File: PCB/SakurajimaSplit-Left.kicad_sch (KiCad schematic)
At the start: 14 parts, among them J1 SWD, J2 USB_C_Receptacle_USB2.0_16P, J3 USB_C_Receptacle_USB2.0_16P, SW22 SW_Push, U1 USBLC6-2SC6, U2 STM32G0B1CBT6, Y1 8MHz

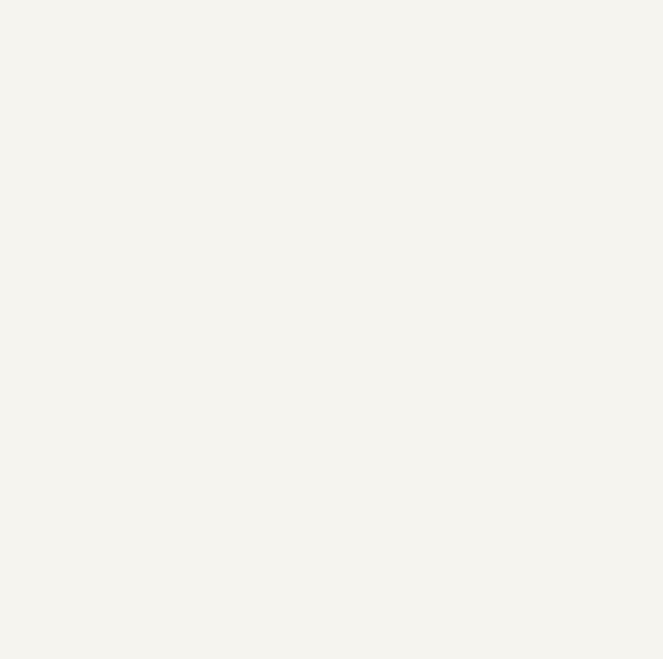
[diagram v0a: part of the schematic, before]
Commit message: feat(schematic): add key matrix
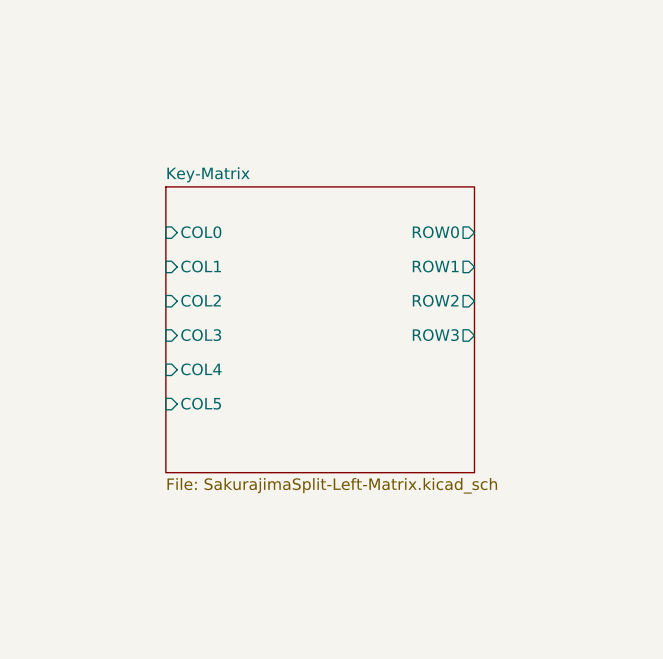
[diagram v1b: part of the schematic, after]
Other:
- added sheet Key-Matrix (SakurajimaSplit-Left-Matrix.kicad_sch)
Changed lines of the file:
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@@
+		)
+	)
+	(sheet
+		(at 227.33 109.22)
+		(size 34.29 31.75)
+		(exclude_from_sim no)
+		(in_bom yes)
+		(on_board yes)
+		(dnp no)
+		(fields_autoplaced yes)
+		(stroke
+			(width 0.1524)
+			(type solid)
+		)
+		(fill
+			(color 0 0 0 0.0000)
+		)
+		(property "Sheetname" "Key-Matrix"
+			(at 227.33 108.5084 0)
+			(effects
+				(font
+					(size 1.27 1.27)
+				)
+				(justify left bottom)
+			)
+		)
+		(property "Sheetfile" "SakurajimaSplit-Left-Matrix.kicad_sch"
+			(at 227.33 141.5546 0)
+			(effects
+				(font
+					(size 1.27 1.27)
+				)
+				(justify left top)
+			)
+		)
+		(pin "ROW0" output
+			(at 261.62 114.3 0)
+			(effects
+				(font
+					(size 1.27 1.27)
+				)
+				(justify right)
+			)
+		)
+		(pin "ROW1" output
+			(at 261.62 118.11 0)
+			(effects
+				(font
+					(size 1.27 1.27)
+				)
+				(justify right)
+			)
+		)
+		(pin "ROW2" output
+			(at 261.62 121.92 0)
+			(effects
+				(font
+					(size 1.27 1.27)
+				)
+				(justify right)
+			)
+		)
+		(pin "ROW3" output
+			(at 261.62 125.73 0)
+			(effects
+				(font
+					(size 1.27 1.27)
+				)
+				(justify right)
+			)
+		)
+		(pin "COL0" input
+			(at 227.33 114.3 180)
+			(effects
+				(font
+					(size 1.27 1.27)
+				)
+				(justify left)
+			)
+		)
+		(pin "COL1" input
+			(at 227.33 118.11 180)
+			(effects
+				(font
+					(size 1.27 1.27)
+				)
+				(justify left)
+			)
+		)
+		(pin "COL2" input
+			(at 227.33 121.92 180)
+			(effects
+				(font
+					(size 1.27 1.27)
+				)
+				(justify left)
+			)
+		)
+		(pin "COL3" input
+			(at 227.33 125.73 180)
+			(effects
+				(font
+					(size 1.27 1.27)
+				)
+				(justify left)
+			)
+		)
+		(pin "COL4" input
+			(at 227.33 129.54 180)
+			(effects
+				(font
+					(size 1.27 1.27)
+				)
+				(justify left)
+			)
+		)
+		(pin "COL5" input
+			(at 227.33 133.35 180)
+			(effects
+				(font
+					(size 1.27 1.27)
+				)
+				(justify left)
+			)
+		)
+		(instances
+			(project "SakurajimaSplit"
+				(path "/2049b6de-7453-46e1-ab60-70116abff9d6/d08add9a-e5d5-49be-809e-a90adb11436d"
+					(page "4")
+				)
+			)
 		)
 	)

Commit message: feat(sch): add host USB connection and power circuit
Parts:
- removed J2: USB_C_Receptacle_USB2.0_16P, symbol Connector:USB_C_Receptacle_USB2.0_16P
- removed R2, R3: 5.1k, symbol Device:R
- removed U1: USBLC6-2SC6, Package_TO_SOT_SMD:SOT-23-6, symbol Power_Protection:USBLC6-2SC6
- C1: renamed from C4; value C -> 20pF
- C2: renamed from C5; value C -> 20pF
- R1: value R -> TBD
- renumbered C1 to C3, C2 to C4, J3 to J2, SW22 to SW1, U2 to U1
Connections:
- net USB_D+ renamed Power/USB_D+
- net USB_D- renamed Power/USB_D-
- no-connect marks 6 -> 4
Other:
- added sheet Power (SakurajimaSplit-Left-Power.kicad_sch)
- note removed: "5v to 3.3v Voltage Regulator"
- note removed: "USB-C to PC"
- moved on the sheet: C1, C2, C3, C4, J1, R1, SW1, Y1

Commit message: feat(sch): add USB to right-half circuit
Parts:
- added D24: User LED, symbol Device:LED
- added R5: 330R, symbol Device:R_Small
- added U4: USBLC6-2SC6, Package_TO_SOT_SMD:SOT-23-6, symbol Power_Protection:USBLC6-2SC6
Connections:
- net GND: now also U1.5 (VREF+), R5.2, U4.2 (GND)
- net VBUS: now reaches J2.A4 (VBUS), J2.A9 (VBUS), J2.B4 (VBUS), J2.B9 (VBUS)
- net VBUS: now also U4.5 (VBUS)
- net at J2.A6 (D+): now also J2.B6 (D+), U4.3 (I/O2)
- net at J2.A7 (D-): now also J2.B7 (D-), U4.1 (I/O1)
- new net: D24.1 (K), R5.1
- new net USART_RX: U4.4 (I/O2)
- new net USART_TX: U4.6 (I/O1)
- new net User_LED: D24.2 (A)
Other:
- note removed: "MCU Decoupling Capacitors"
- moved on the sheet: C1, C2, C3, C4, J1, J2, R1, SW1, U1, Y1

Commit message: feat(sch): add rotary encoder
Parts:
- added C10, C8, C9: 100nF, symbol Device:C
- added R10, R11, R6, R7, R8, R9: 10k, symbol Device:R_Small
- added SW23: Knob, symbol Device:RotaryEncoder_Switch
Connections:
- net +3.3V: now also R6.2, R7.2, R8.2
- net GND: now also C10.2, C8.2, C9.2, SW23.S2
- new net: R6.1, R9.2, SW23.A
- new net: R10.2, R7.1, SW23.B
- new net: R11.2, R8.1, SW23.S1
- new net Knob_A: C10.1, R9.1
- new net Knob_B: C8.1, R10.1
- new net Knob_SW: C9.1, R11.1
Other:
- moved on the sheet: C3, C4, U1

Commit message: feat(sch): add OLED display
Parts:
- removed J1: SWD, symbol Connector:Conn_01x05_Pin
- added J4: SWD, symbol Connector_Generic:Conn_01x05
- added U5: ZJY_M233, Hayata_Lib:OLED_SSD1305, symbol Hayata_Lib:OLED_SSD1305
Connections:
- net +3.3V: now also J4.1 (Pin_1), U5.2 (3.3V)
- net GND: now also J4.5 (Pin_5), U5.1 (GND)
- net NRST: now also J4.4 (Pin_4)
- net SWCLK/BOOT0: now also J4.3 (Pin_3)
- net SWDIO: now also J4.2 (Pin_2)
- net User_LED renamed CapsLock
- new net Display_DC: U5.6 (DC)
- new net Display_SCLK: U5.3 (SCL/SCLK)
- new net Display_SDI: U5.4 (SDA/SDIN)
- new net Display_~{CS}: U5.7 (~{CS})
- new net Display_~{EN}: U5.8 (~{EN})
- new net Display_~{RST}: U5.5 (~{RST})
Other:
- note added: "CapsLock ind."
- note removed: "LED Underglow"
- note removed: "User LED"

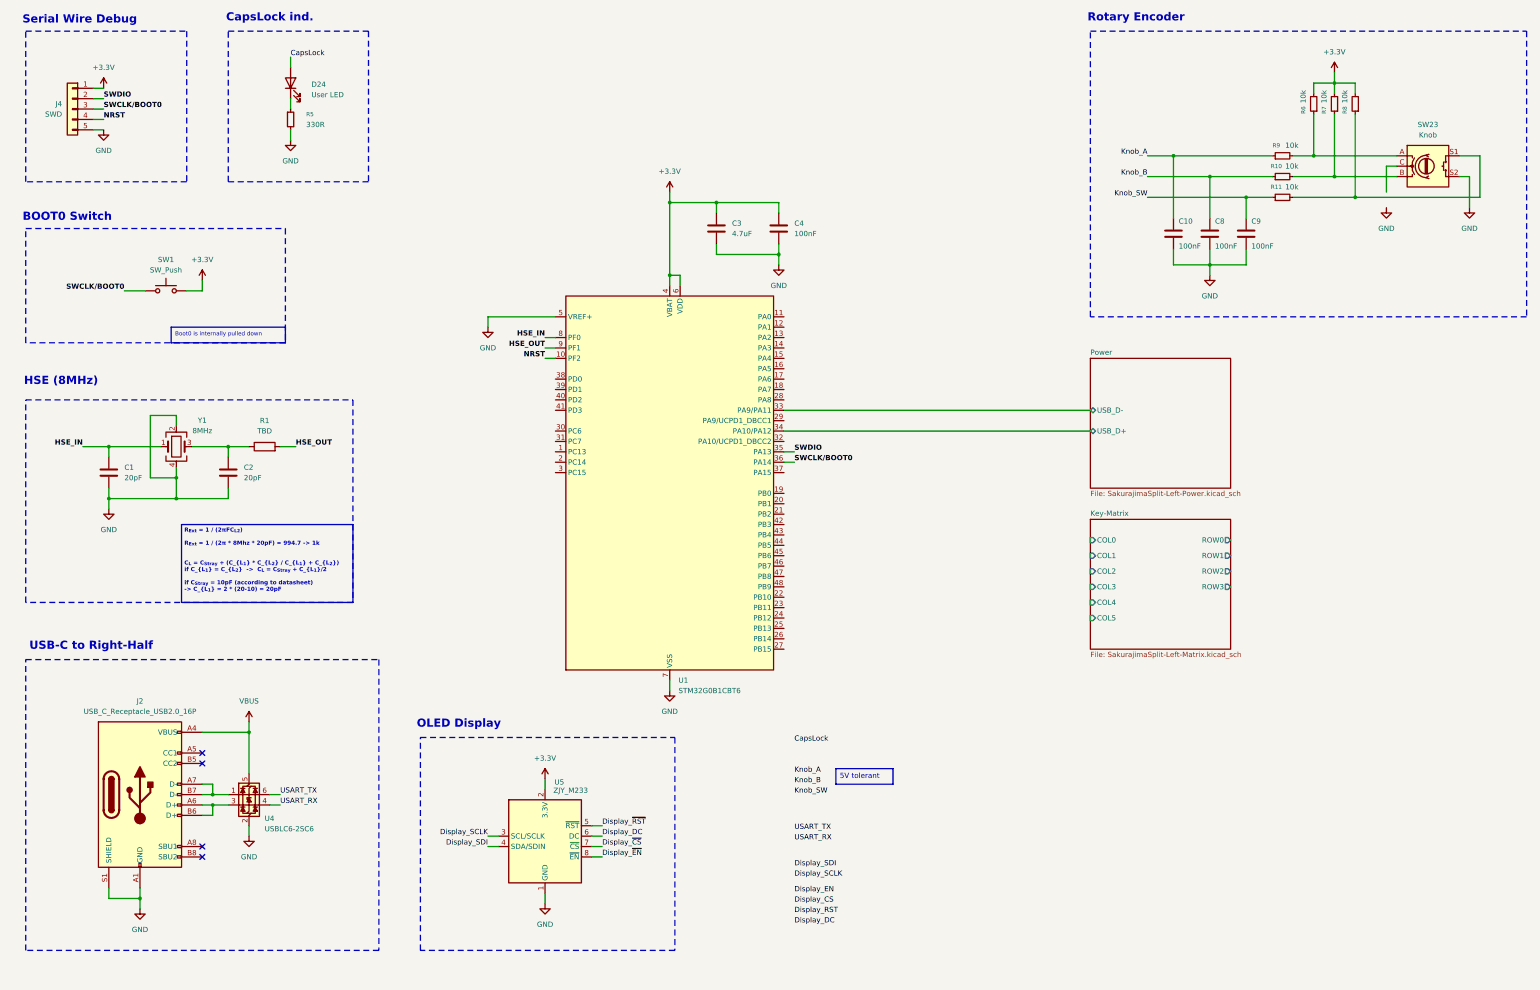
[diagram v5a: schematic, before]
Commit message: feat(sch): mcu connections, test points and schematic cleanup
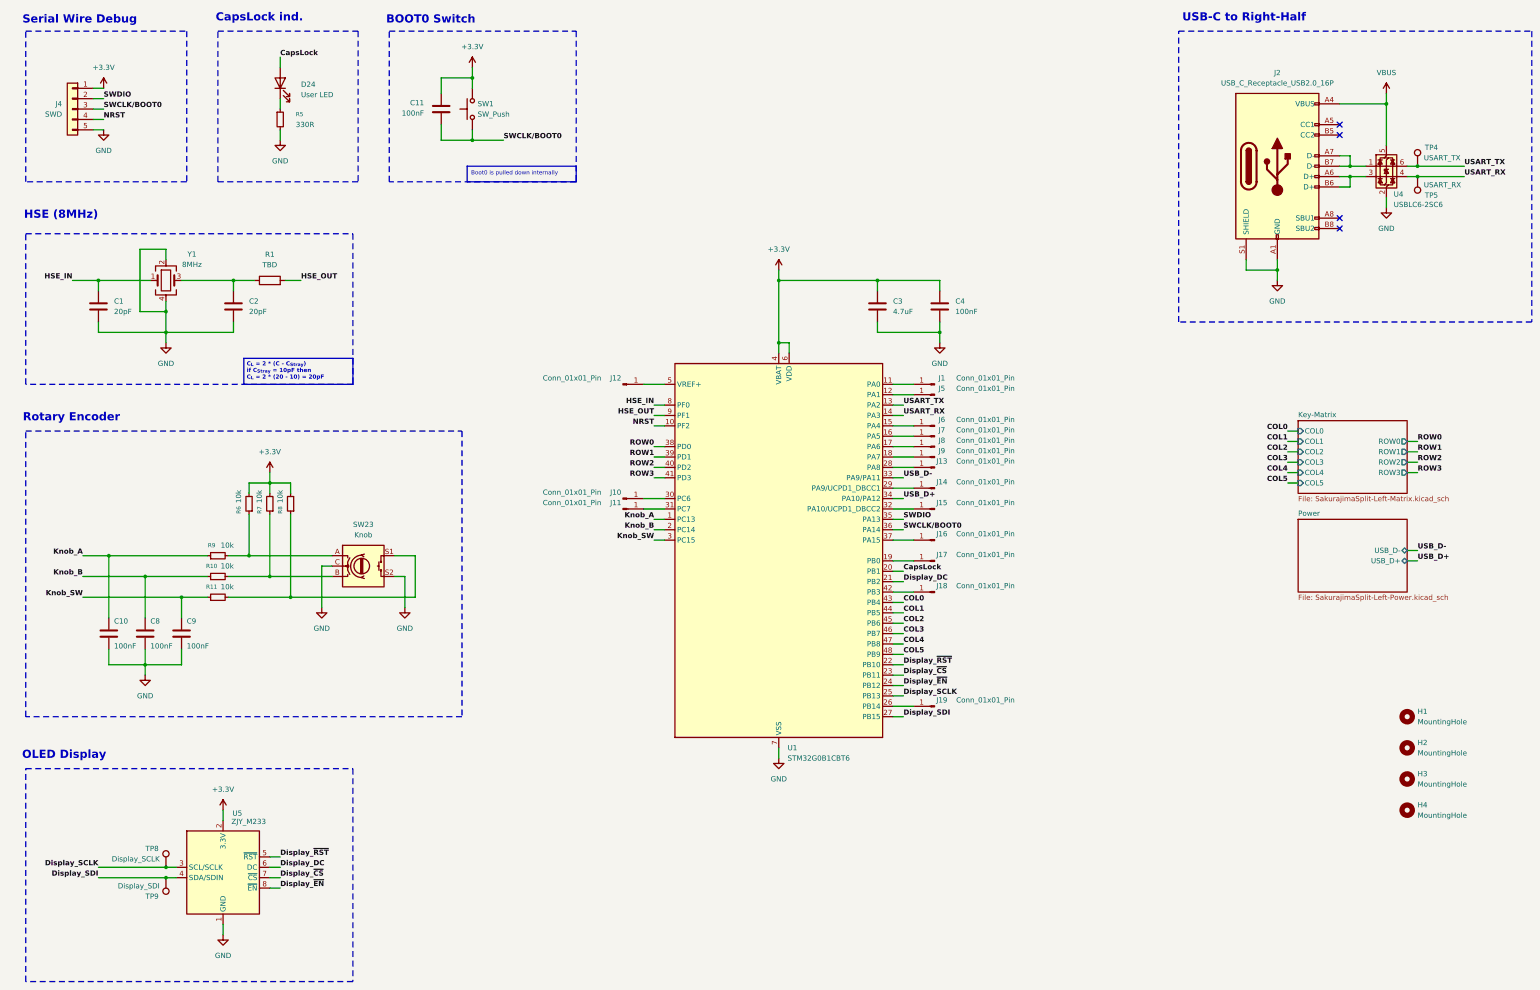
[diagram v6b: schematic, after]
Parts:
- added C11: 100nF, symbol Device:C
- added H1, H2, H3, H4: MountingHole, symbol Mechanical:MountingHole
- added J1, J10, J11, J12, J13, J14, J15, J16, J17, J18, J19, J6, J7, J8, J9: Conn_01x01_Pin, symbol Connector:Conn_01x01_Pin
- added J5: Conn_01x01_Pin, Connector_Wire:SolderWirePad_1x01_SMD_1x2mm, symbol Connector:Conn_01x01_Pin
- added TP4: USART_TX, symbol Connector:TestPoint
- added TP5: USART_RX, symbol Connector:TestPoint
- added TP8: Display_SCLK, symbol Connector:TestPoint
- added TP9: Display_SDI, symbol Connector:TestPoint
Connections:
- net +3.3V: now also C11.1
- net CapsLock: now also U1.20 (PB1)
- net Display_DC: now also U1.21 (PB2)
- net Display_SCLK: now also U1.25 (PB13), TP8.1
- net Display_SDI: now also U1.27 (PB15), TP9.1
- net Display_~{CS}: now also U1.23 (PB11)
- net Display_~{EN}: now also U1.24 (PB12)
- net Display_~{RST}: now also U1.22 (PB10)
- net GND: now also SW23.C; no longer U1.5 (VREF+)
- net Knob_A: now also U1.1 (PC13)
- net Knob_B: now also U1.2 (PC14)
- net Knob_SW: now also U1.3 (PC15)
- net SWCLK/BOOT0: now also C11.2
- net USART_RX: now also U1.14 (PA3), TP5.1
- net USART_TX: now also U1.13 (PA2), TP4.1
- net at U1.11 (PA0): now also J1.1 (Pin_1)
- net at U1.12 (PA1): now also J5.1 (Pin_1)
- net at U1.15 (PA4): now also J6.1 (Pin_1)
- net at U1.16 (PA5): now also J7.1 (Pin_1)
- net at U1.17 (PA6): now also J8.1 (Pin_1)
- net at U1.18 (PA7): now also J9.1 (Pin_1)
- net at U1.19 (PB0): now also J17.1 (Pin_1)
- net at U1.26 (PB14): now also J19.1 (Pin_1)
- net at U1.28 (PA8): now also J13.1 (Pin_1)
- net at U1.29 (PA9/UCPD1_DBCC1): now also J14.1 (Pin_1)
- net at U1.30 (PC6): now also J10.1 (Pin_1)
- net at U1.31 (PC7): now also J11.1 (Pin_1)
- net at U1.32 (PA10/UCPD1_DBCC2): now also J15.1 (Pin_1)
- net at U1.37 (PA15): now also J16.1 (Pin_1)
- net ROW0: now reaches U1.38 (PD0)
- net ROW1: now reaches U1.39 (PD1)
- net ROW2: now reaches U1.40 (PD2)
- net ROW3: now reaches U1.41 (PD3)
- net at U1.42 (PB3): now also J18.1 (Pin_1)
- net COL0: now reaches U1.43 (PB4)
- net COL1: now reaches U1.44 (PB5)
- net COL2: now reaches U1.45 (PB6)
- net COL3: now reaches U1.46 (PB7)
- net COL4: now reaches U1.47 (PB8)
- net COL5: now reaches U1.48 (PB9)
- net Power/USB_D+ renamed USB_D+
- net Power/USB_D- renamed USB_D-
- new net: J12.1 (Pin_1), U1.5 (VREF+)
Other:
- moved on the sheet: C1, C10, C2, C3, C4, C8, C9, D24, J2, R1, R10, R11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
